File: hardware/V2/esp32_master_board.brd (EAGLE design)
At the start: 65 x 35 mm, 62 parts, among them IC1 SN74HC138PW, IC2 MAX17502EATB+T, SW1 B3U-1000P-2P-SMD

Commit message: [HARDWARE] Continue V2 design
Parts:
- added IC3, IC4: WS2812B, WS2812B:WS2812B
- added U$5: DF13-3P-1.25DSA, con-hirose-df13:DF13-3P-1.25DSA
- added U$6: DF13-4P-1.25DSA, con-hirose-df13:DF13-4P-1.25DSA
- C10: device resistor:C0805K -> resistor:C1210
- C17: value 1u -> 22u
- U$4: value DF13-7P-1.25DSA -> DF13-6P-1.25DSA; device con-hirose-df13:DF13-7P-1.25DSA -> con-hirose-df13:DF13-6P-1.25DSA
- moved R6 7.75 mm to (33.0, 5.40), turned to 90 degrees
- moved C2 5.11 mm to (35.2, 5.24)
- moved C3 5.02 mm to (35.2, 6.35)
- moved C6 3.98 mm to (27.6, 15.2), turned to 0 degrees
- moved R8 3.33 mm to (24.1, 8.73)
- moved R9 3.33 mm to (24.1, 7.46)
- moved R12 2.38 mm to (24.1, 10.0)
- moved R10 2.22 mm to (24.1, 13.3)
- moved R13 2.22 mm to (24.1, 12.1)
- moved R11 1.90 mm to (24.1, 15.2)
- moved C1 1.75 mm to (24.1, 16.4)
- moved C13 1.60 mm to (49.7, 25.4)
- moved C5 1.59 mm to (24.1, 17.5)
- moved R14 1.56 mm to (57.3, 9.21)
- moved R7 1.46 mm to (27.8, 8.57), turned to 0 degrees
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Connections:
- removed net I35: U$1.IO35, U$4.P$3
- removed net IO32: U$1.IO32, U$4.P$5
- new net I35_RX1: U$1.IO35, U$6.P$2
- new net IO32_TX1: U$1.IO32, U$6.P$3
- new net N$19: IC3.2, IC4.4
- new net WSLED_OUT: IC4.2, U$5.P$3
- net 5V: now also IC3.1, IC4.1, U$4.P$5, U$5.P$2, U$6.P$4
- net GND: now also IC3.3, IC4.3, U$5.P$1, U$6.P$1
- net IO2: now also IC3.4, U$4.P$3; no longer U$4.P$4
- net IO33: now also U$4.P$4; no longer U$4.P$6
- net VCC: now also U$4.P$6; no longer U$4.P$7
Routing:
- net 5V: track 8.72 -> 64.1 mm, vias 2 -> 5
- net N$19: track 0.00 -> 35.3 mm, vias 0 -> 1
- net IO32_TX1: track 0.00 -> 16.0 mm, vias 0 -> 1
- net WSLED_OUT: track 0.00 -> 15.0 mm
- net I35_RX1: track 0.00 -> 14.9 mm, vias 0 -> 1
- net VCC: track 127.1 -> 118.9 mm, vias 8 -> 7
- net CLK50: track 29.8 -> 37.1 mm
- net N$5: track 9.35 -> 2.52 mm
- net IO32: track 5.58 -> 0.00 mm
- net N$14: track 8.42 -> 3.14 mm
- net I35: track 5.07 -> 0.00 mm
- net N$25: track 36.8 -> 40.6 mm
- net RST: track 33.3 -> 29.6 mm
- net GND: track 19.8 -> 22.8 mm, vias 48 -> 63
- net N$16: track 6.65 -> 8.54 mm
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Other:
- board text added: "5V"
- board text added: "I35/RX1"
- board text added: "IO32/TX1"
- board text added: "WS_LED"
- board text added: "github.com/open-dynamic-robot-initiative"
- board text removed: "I35"
- board text removed: "IO32"
- board text removed: "SOLO MASTER BOARD V01 - LAAS CNRS"

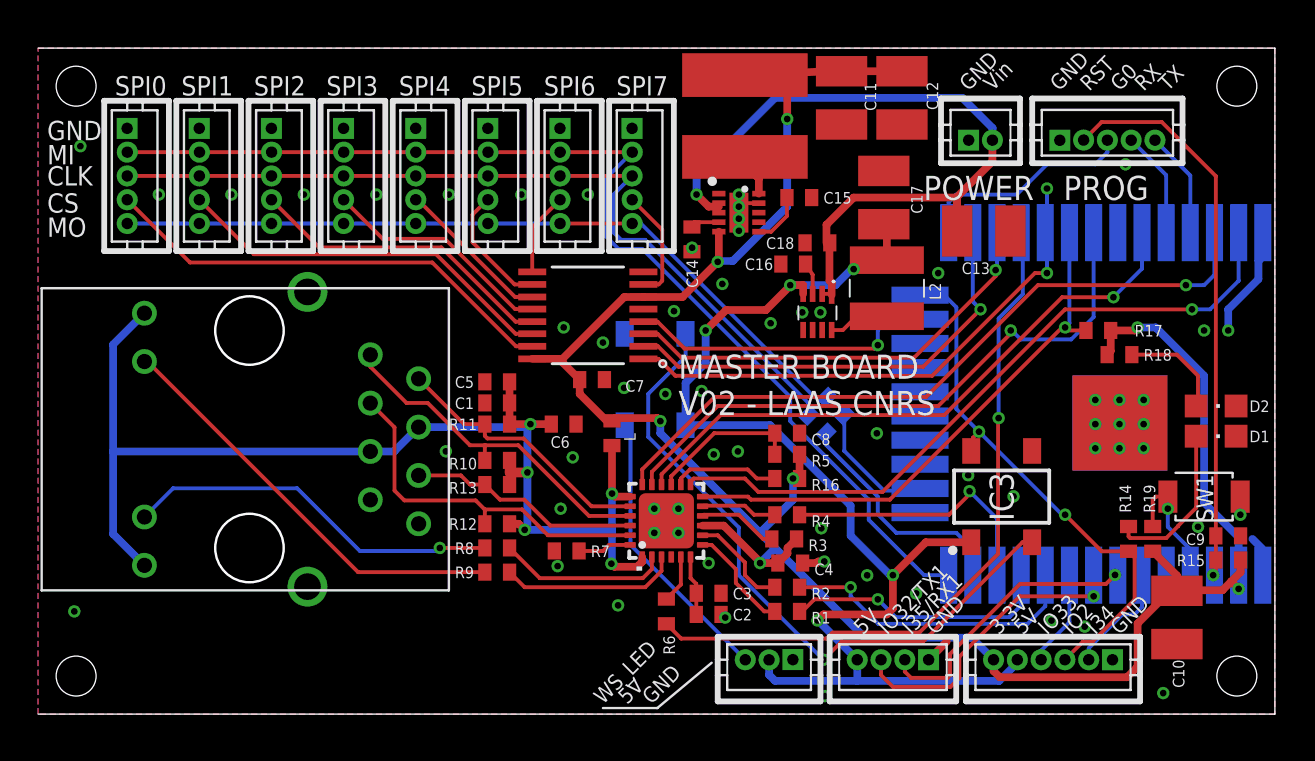
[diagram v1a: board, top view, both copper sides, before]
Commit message: [HARDWARE] simplify design of the V2 removing the 5V since IMU is ok with 3.3V. WS2812 LEDs are out of spec for 3.3V but works in practice. The LED are not critical, and 5V LED would require a level shifter
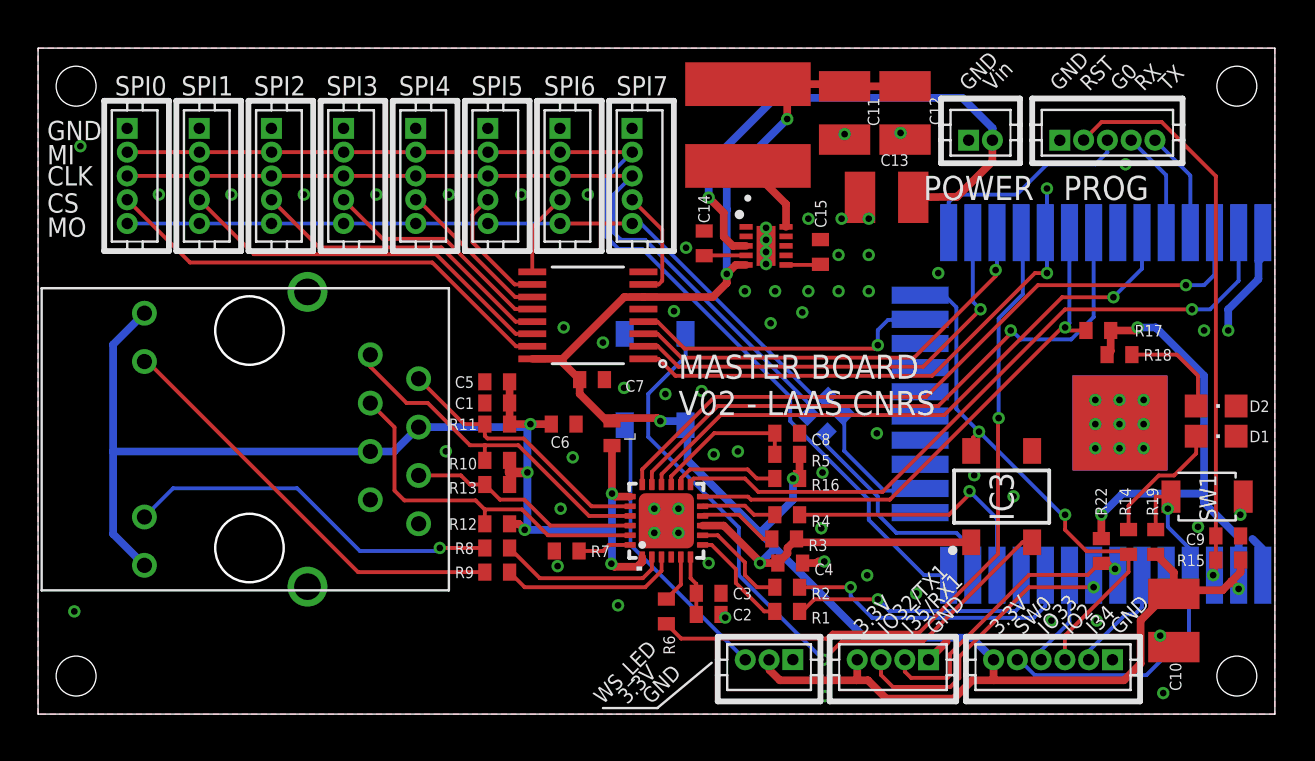
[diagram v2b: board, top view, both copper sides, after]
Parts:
- removed C16, C18: 1u, resistor:C0402
- removed C17: 22u, resistor:C1210
- removed L2: LPS4018-473ML, LPS4018-333MRC:LPS4018223MRC
- removed PS1: MAX15062AATA+T, MAX15062AATA:MAX14591ETAT
- added R22: 4.7k, resistor:R0402
- moved C13 5.40 mm to (44.6, 27.2), turned to 180 degrees
- moved C15 3.07 mm to (41.1, 24.3), turned to 90 degrees
- moved IC2 2.26 mm to (38.3, 24.6)
- moved C11 0.81 mm to (42.4, 31.6)
- moved C12 0.81 mm to (45.6, 31.6)
- moved C14 0.67 mm to (35.0, 24.7), turned to 270 degrees
- moved L1 0.50 mm to (37.3, 31.0)
- moved C10 0.22 mm to (59.7, 4.92)
- moved R19 0.22 mm to (58.7, 9.05)
- moved R14 0.16 mm to (57.3, 9.05)
- moved SW1 0.16 mm to (61.4, 11.4)
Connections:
- removed net 5V: C17.2, IC3.1, IC4.1, L2.2, PS1.4, U$4.P$5, U$5.P$2, U$6.P$4
- removed net N$22: L2.1, PS1.8
- removed net N$24: C16.2, PS1.3
- net GND: no longer C16.1, C17.1, C18.1, PS1.7
- net I35_RX1: now also R22.2
- net N$25: no longer C18.2, PS1.1, PS1.2
- net SW0: now also U$4.P$5
- net VCC: now also IC3.1, IC4.1, R22.1, U$5.P$2, U$6.P$4
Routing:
- net 5V: track 64.1 -> 0.00 mm, vias 5 -> 0
- net VCC: track 118.9 -> 154.8 mm, vias 7 -> 8
- net SW0: track 6.90 -> 20.5 mm
- net N$25: track 40.6 -> 29.2 mm
- net N$22: track 3.20 -> 0.00 mm
- net N$18: track 2.23 -> 4.03 mm
- net N$16: track 8.54 -> 6.85 mm
- net N$24: track 1.68 -> 0.00 mm
- net GND: track 22.8 -> 21.4 mm, vias 63 -> 75
- net I35_RX1: track 14.9 -> 15.9 mm
- net N$23: track 2.78 -> 1.82 mm
- net N$15: track 1.57 -> 2.21 mm
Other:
- board text added: "SW0"
- board text removed: "5V"

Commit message: [hardware] increase clearance around the holes, minor changes
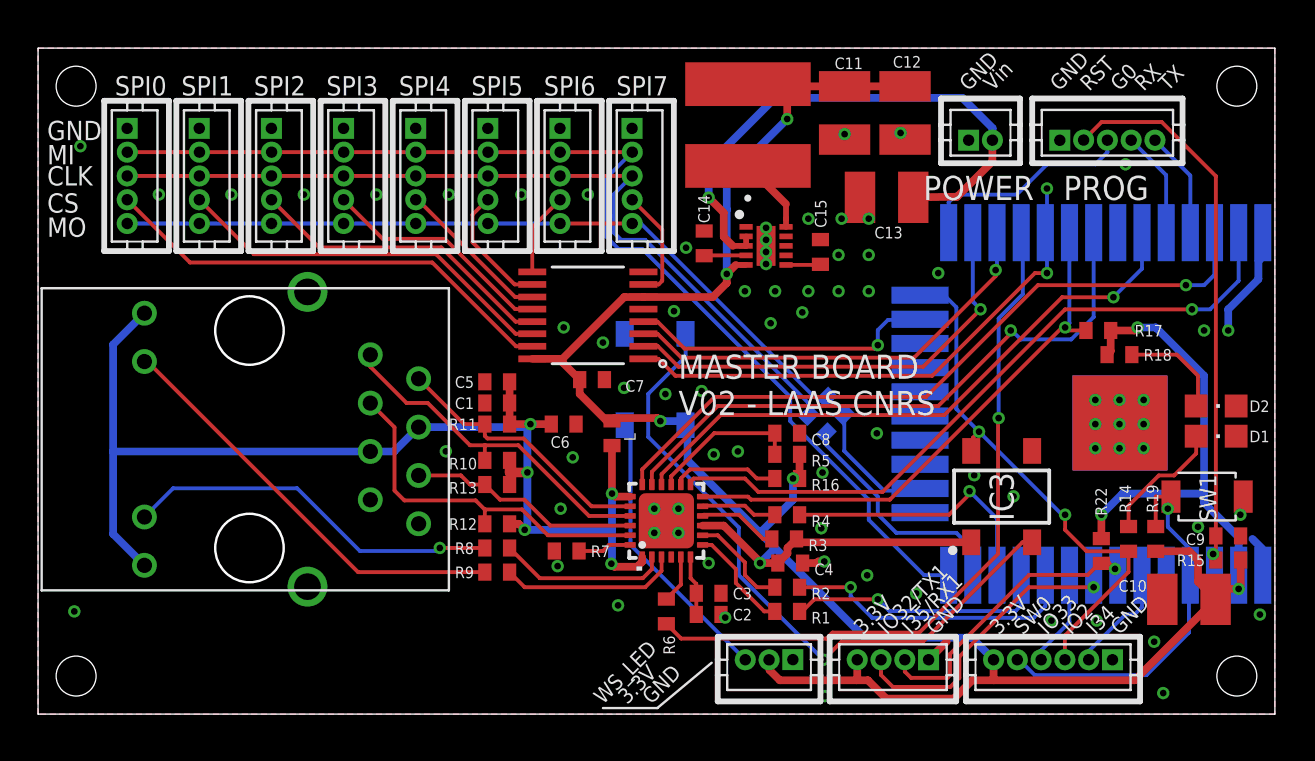
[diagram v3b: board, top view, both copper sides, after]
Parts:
- C10: value 100n -> 10u
- moved C10 1.37 mm to (60.5, 6.03), turned to 180 degrees
- moved R14 0.16 mm to (57.3, 9.21)
- moved R19 0.16 mm to (58.7, 9.21)
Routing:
- net VCC: track 154.8 -> 151.3 mm
- net RST: track 29.6 -> 30.2 mm
- net N$25: track 29.2 -> 29.7 mm
- net GND: vias 75 -> 76

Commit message: [hardware] V2.1: Add MPN for all parts, fix some footprints, add BOM compatible with seeedfusion PCBA, add pick and place files
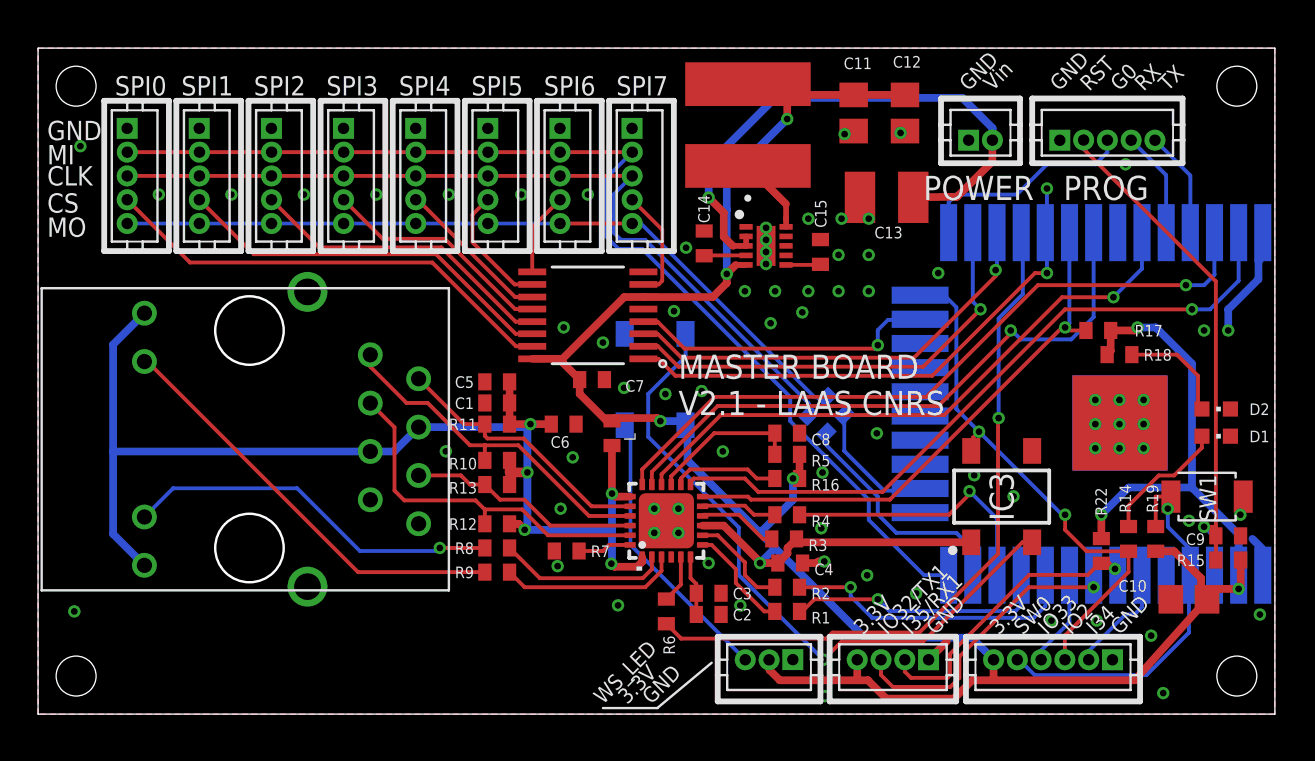
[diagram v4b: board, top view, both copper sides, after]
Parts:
- C10: value 10u -> 22u; device resistor:C1210 -> rcl:C0805
- C11, C12: device resistor:C1210 -> rcl:C0805
- D1, D2: device led:CHIPLED_0805 -> led:CHIPLED_0603
- L: value (none) -> 0
- L1: value 33uH -> 15uH; device LPS6235-682MRB:LPS6235 -> LPS6235-153MRB:LPS6235
- moved C11 0.48 mm to (42.9, 31.6)
- moved D2 0.16 mm to (61.9, 16.0)
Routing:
- net VCC: track 151.3 -> 148.2 mm
- net GND: vias 76 -> 75
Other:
- board text added: "MASTER BOARD V2.1 - LAAS CNRS"
- board text removed: "MASTER BOARD V02 - LAAS CNRS"

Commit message: Small trace path changes to prevent possible shorting of MISO line due to sharp grounded ESP32 module corner, small optimisations
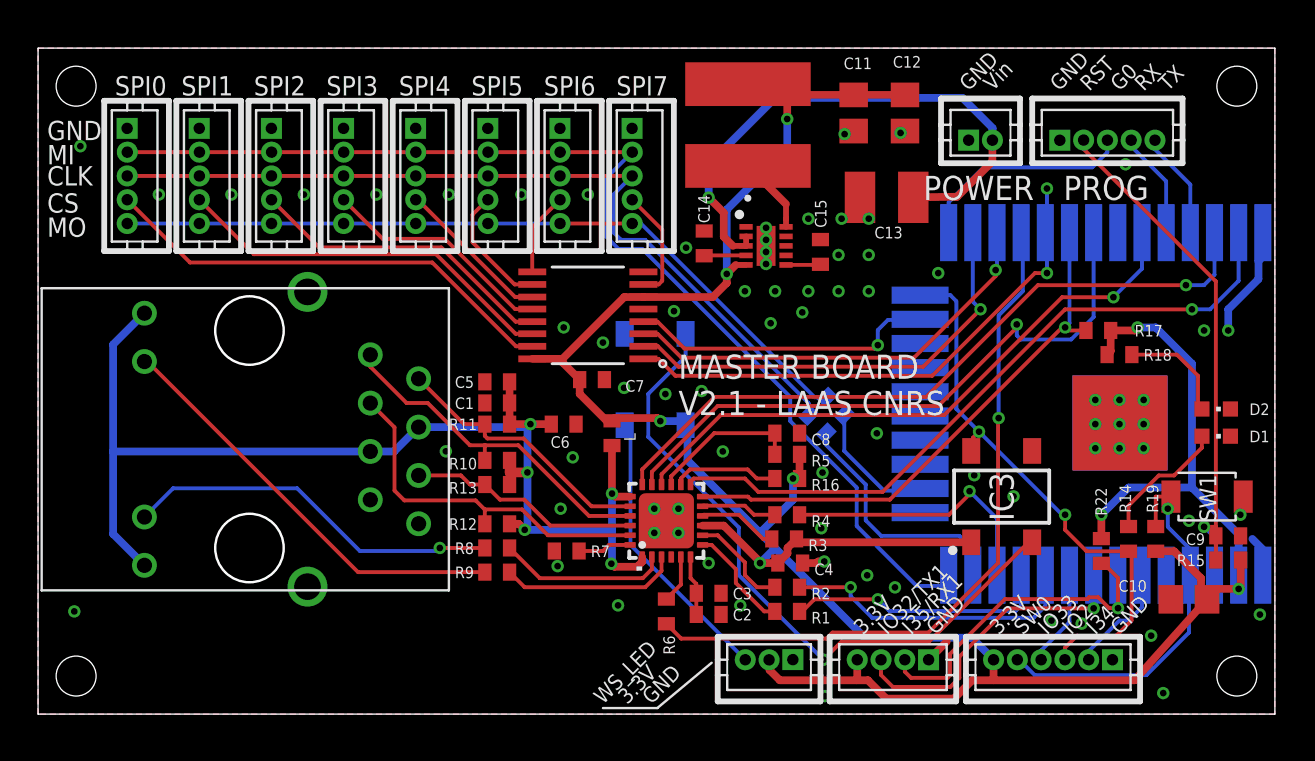
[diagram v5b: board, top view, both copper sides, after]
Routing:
- net I35_RX1: track 15.9 -> 19.1 mm
- net IO2: track 28.4 -> 29.9 mm
- net SPI_MISO: track 58.3 -> 59.6 mm
- net IO32_TX1: track 15.7 -> 16.3 mm
- net TXD0: track 32.2 -> 32.8 mm
- net N$21: track 12.5 -> 13.1 mm

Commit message: [Hardware] move via away from exposed pad, add fiducials, minor component location changes
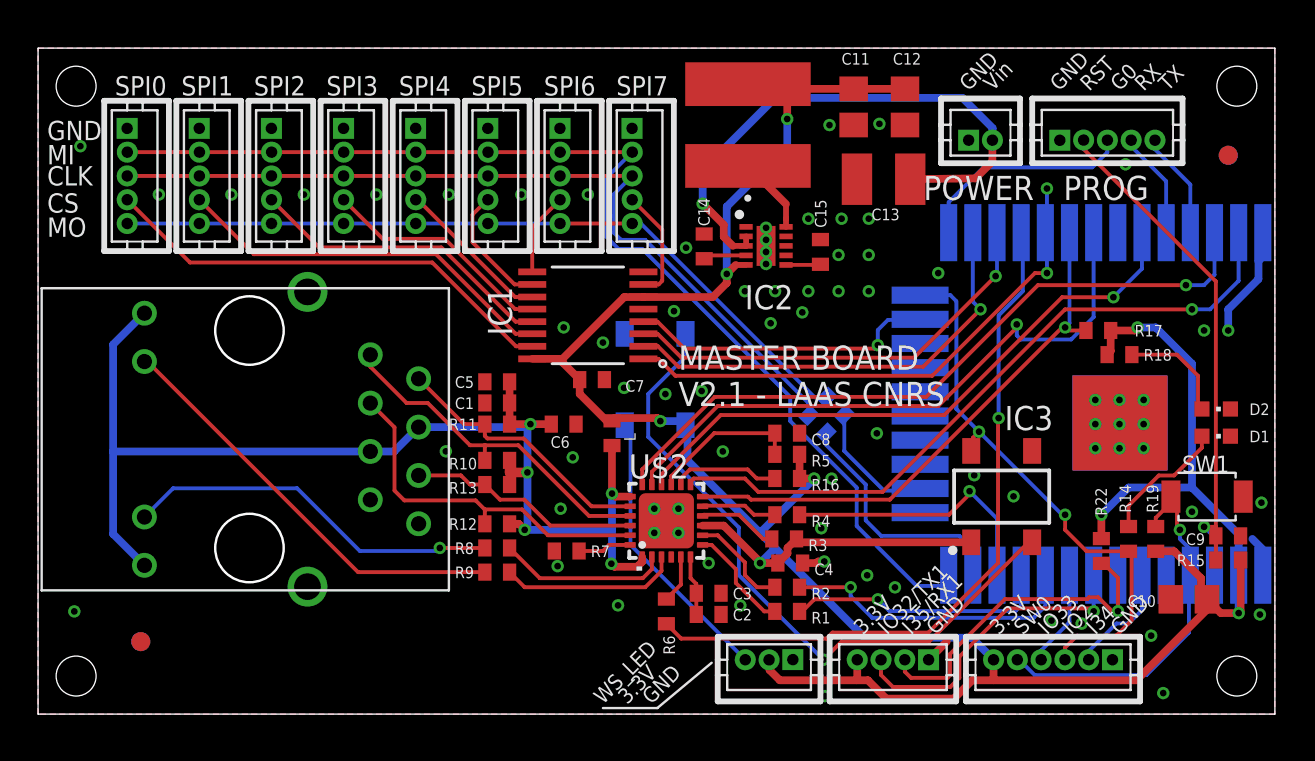
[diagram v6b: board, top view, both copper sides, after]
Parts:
- added REF1, REF2, REF3, REF4: (no value), dicons:VISION_REF10
- moved C13 0.97 mm to (44.4, 28.1)
- moved C11 0.32 mm to (42.9, 31.9)
- moved C12 0.32 mm to (45.6, 31.9)
- moved C14 0.16 mm to (35.0, 24.6)
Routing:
- net VCC: track 148.2 -> 153.9 mm
- net SW0: track 20.4 -> 19.8 mm
